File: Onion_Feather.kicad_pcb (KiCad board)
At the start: 2 copper layers, 50.8 x 53.3 mm, 2 parts, among them U1 Omega2+

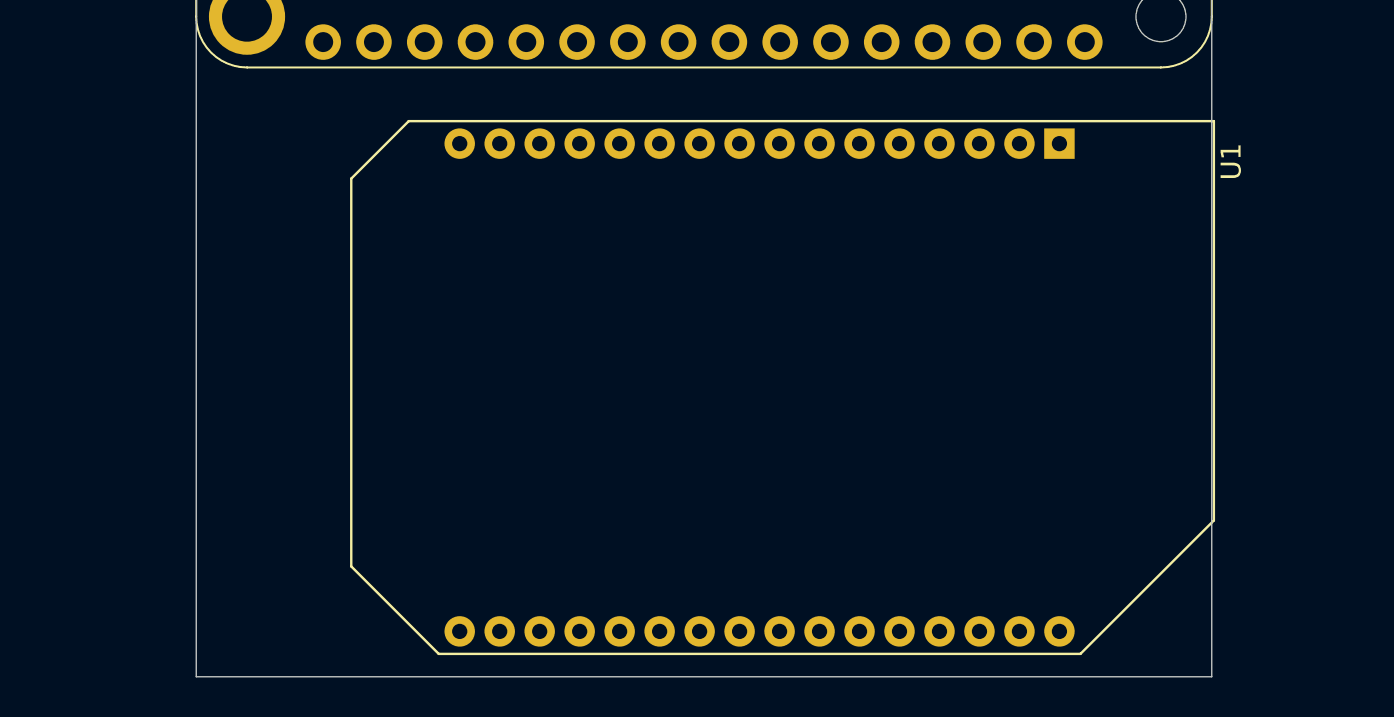
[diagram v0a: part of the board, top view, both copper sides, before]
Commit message: Add Hanrun magjack
Signed-off-by: Tisham Dhar <whatnickd@gmail.com>
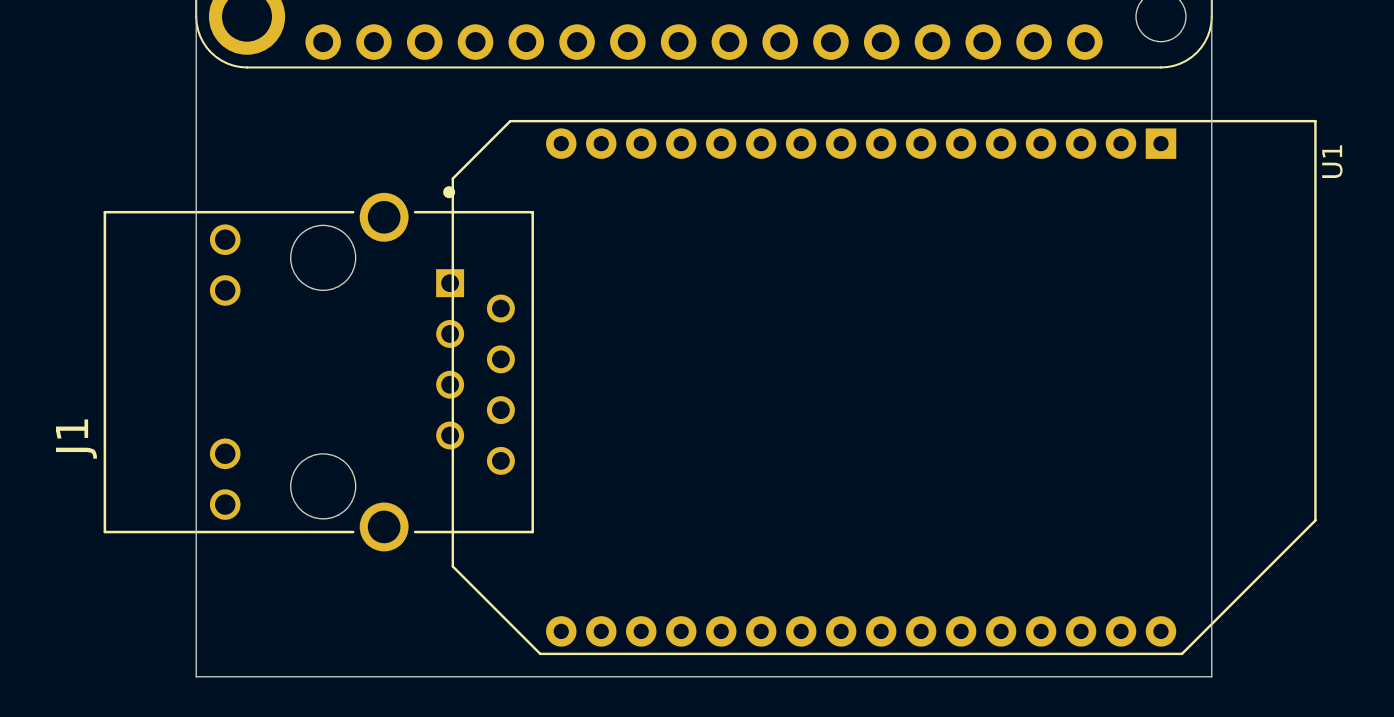
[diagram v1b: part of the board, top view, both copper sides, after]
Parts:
- added J1: HR911105A, footprints:HANRUN_HR911105A, F.Cu at (123.2, 99.1)
- moved U1 5.08 mm to (165.1, 87.6)
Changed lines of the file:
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@@
     (tracks 0)
     (zones 0)
-    (modules 2)
-    (nets 60)
+    (modules 3)
+    (nets 72)
   )
   (page A4)
@@
   (net 58 "Net-(U1-Pad3)")
   (net 59 "Net-(U1-Pad2)")
+  (net 60 "Net-(J1-Pad15)")
+  (net 61 "Net-(J1-Pad11)")
+  (net 62 "Net-(J1-Pad12)")
+  (net 63 "Net-(J1-Pad10)")
+  (net 64 "Net-(J1-Pad9)")
+  (net 65 "Net-(J1-Pad8)")
+  (net 66 "Net-(J1-Pad6)")
+  (net 67 "Net-(J1-Pad5)")
+  (net 68 "Net-(J1-Pad4)")
+  (net 69 "Net-(J1-Pad3)")
+  (net 70 "Net-(J1-Pad2)")
+  (net 71 "Net-(J1-Pad1)")
   (net_class Default "This is the default net class."
     (clearance 0.2)
@@
     (uvia_dia 0.3)
     (uvia_drill 0.1)
+    (add_net "Net-(J1-Pad1)")
+    (add_net "Net-(J1-Pad10)")
+    (add_net "Net-(J1-Pad11)")
+    (add_net "Net-(J1-Pad12)")
+    (add_net "Net-(J1-Pad15)")
+    (add_net "Net-(J1-Pad2)")
+    (add_net "Net-(J1-Pad3)")
+    (add_net "Net-(J1-Pad4)")
+    (add_net "Net-(J1-Pad5)")
+    (add_net "Net-(J1-Pad6)")
+    (add_net "Net-(J1-Pad8)")
+    (add_net "Net-(J1-Pad9)")
     (add_net "Net-(MS1-Pad1)")
     (add_net "Net-(MS1-Pad10)")
@@
     (add_net "Net-(U1-Pad9)")
   )
+  (module footprints:HANRUN_HR911105A (layer F.Cu)
+    (at 123.19 99.06 90)
+    (fp_text reference J1 (at -3.18815 -12.50276 90) (layer F.SilkS)
+      (effects (font (size 1.607654 1.607654) (thickness 0.015)))
+    )
+    (fp_text value HR911105A (at 8.02765 12.354385 90) (layer F.Fab)
+      (effects (font (size 1.605063 1.605063) (thickness 0.015)))
+    )
+    (fp_line (start 9.25 -11.17) (end -9.25 -11.17) (layer F.CrtYd) (width 0.05))
+    (fp_line (start 9.25 10.73) (end 9.25 -11.17) (layer F.CrtYd) (width 0.05))
+    (fp_line (start -9.25 10.73) (end 9.25 10.73) (layer F.CrtYd) (width 0.05))
+    (fp_line (start -9.25 -11.17) (end -9.25 10.73) (layer F.CrtYd) (width 0.05))
+    (fp_line (start 8 -10.92) (end -8 -10.92) (layer F.Fab) (width 0.127))
+    (fp_line (start 8 10.48) (end 8 -10.92) (layer F.Fab) (width 0.127))
+    (fp_line (start -8 10.48) (end 8 10.48) (layer F.Fab) (width 0.127))
+    (fp_line (start -8 -10.92) (end -8 10.48) (layer F.Fab) (width 0.127))
+    (fp_circle (center 9 6.3) (end 9.15 6.3) (layer F.SilkS) (width 0.3))
+    (fp_circle (center 5.8 6.3) (end 5.95 6.3) (layer F.Fab) (width 0.3))
+    (fp_line (start 8 4.6) (end 8 10.48) (layer F.SilkS) (width 0.127))
+    (fp_line (start 8 -10.92) (end 8 1.5) (layer F.SilkS) (width 0.127))
+    (fp_line (start -8 4.6) (end -8 10.48) (layer F.SilkS) (width 0.127))
+    (fp_line (start -8 -10.92) (end -8 1.5) (layer F.SilkS) (width 0.127))
+    (fp_line (start 8 -10.92) (end -8 -10.92) (layer F.SilkS) (width 0.127))
+    (fp_line (start 8 10.48) (end -8 10.48) (layer F.SilkS) (width 0.127))
+    (pad None np_thru_hole circle (at 5.715 0 90) (size 3.25 3.25) (drill 3.25) (layers *.Cu *.Mask))
+    (pad None np_thru_hole circle (at -5.715 0 90) (size 3.25 3.25) (drill 3.25) (layers *.Cu *.Mask))
+    (pad 16 thru_hole circle (at -7.745 3.05 90) (size 2.445 2.445) (drill 1.63) (layers *.Cu *.Mask)
+      (net 60 "Net-(J1-Pad15)"))
+    (pad 15 thru_hole circle (at 7.745 3.05 90) (size 2.445 2.445) (drill 1.63) (layers *.Cu *.Mask)
+      (net 60 "Net-(J1-Pad15)"))
+    (pad 11 thru_hole circle (at -4.085 -4.9 90) (size 1.53 1.53) (drill 1.02) (layers *.Cu *.Mask)
+      (net 61 "Net-(J1-Pad11)"))
+    (pad 12 thru_hole circle (at -6.625 -4.9 90) (size 1.53 1.53) (drill 1.02) (layers *.Cu *.Mask)
+      (net 62 "Net-(J1-Pad12)"))
+    (pad 10 thru_hole circle (at 4.085 -4.9 90) (size 1.53 1.53) (drill 1.02) (layers *.Cu *.Mask)
+      (net 63 "Net-(J1-Pad10)"))
+    (pad 9 thru_hole circle (at 6.625 -4.9 90) (size 1.53 1.53) (drill 1.02) (layers *.Cu *.Mask)
+      (net 64 "Net-(J1-Pad9)"))
+    (pad 8 thru_hole circle (at -4.44 8.89 90) (size 1.398 1.398) (drill 0.89) (layers *.Cu *.Mask)
+      (net 65 "Net-(J1-Pad8)"))
+    (pad 7 thru_hole circle (at -3.17 6.35 90) (size 1.398 1.398) (drill 0.89) (layers *.Cu *.Mask))
+    (pad 6 thru_hole circle (at -1.9 8.89 90) (size 1.398 1.398) (drill 0.89) (layers *.Cu *.Mask)
+      (net 66 "Net-(J1-Pad6)"))
+    (pad 5 thru_hole circle (at -0.63 6.35 90) (size 1.398 1.398) (drill 0.89) (layers *.Cu *.Mask)
+      (net 67 "Net-(J1-Pad5)"))
+    (pad 4 thru_hole circle (at 0.64 8.89 90) (size 1.398 1.398) (drill 0.89) (layers *.Cu *.Mask)
+      (net 68 "Net-(J1-Pad4)"))
+    (pad 3 thru_hole circle (at 1.91 6.35 90) (size 1.398 1.398) (drill 0.89) (layers *.Cu *.Mask)
+      (net 69 "Net-(J1-Pad3)"))
+    (pad 2 thru_hole circle (at 3.18 8.89 90) (size 1.398 1.398) (drill 0.89) (layers *.Cu *.Mask)
+      (net 70 "Net-(J1-Pad2)"))
+    (pad 1 thru_hole rect (at 4.45 6.35 90) (size 1.398 1.398) (drill 0.89) (layers *.Cu *.Mask)
+      (net 71 "Net-(J1-Pad1)"))
+  )
   (module Module:Onion_Omega2+ (layer F.Cu)
-    (at 160.02 87.63 270)
+    (at 165.1 87.63 270)
     (descr https://onion.io/omega2/)
     (tags "Omega Onion module")

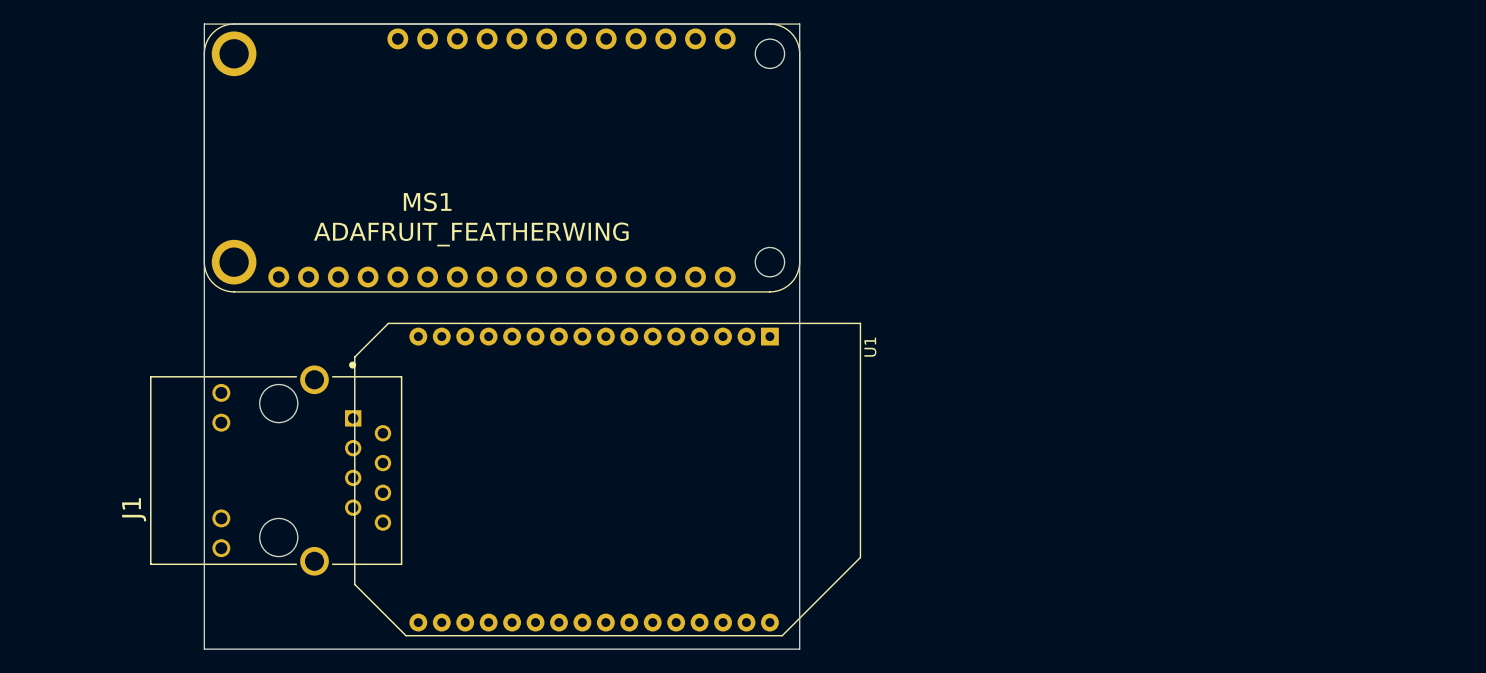
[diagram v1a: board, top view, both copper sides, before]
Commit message: Try Hanrun magjack on for size
Signed-off-by: Tisham Dhar <whatnickd@gmail.com>
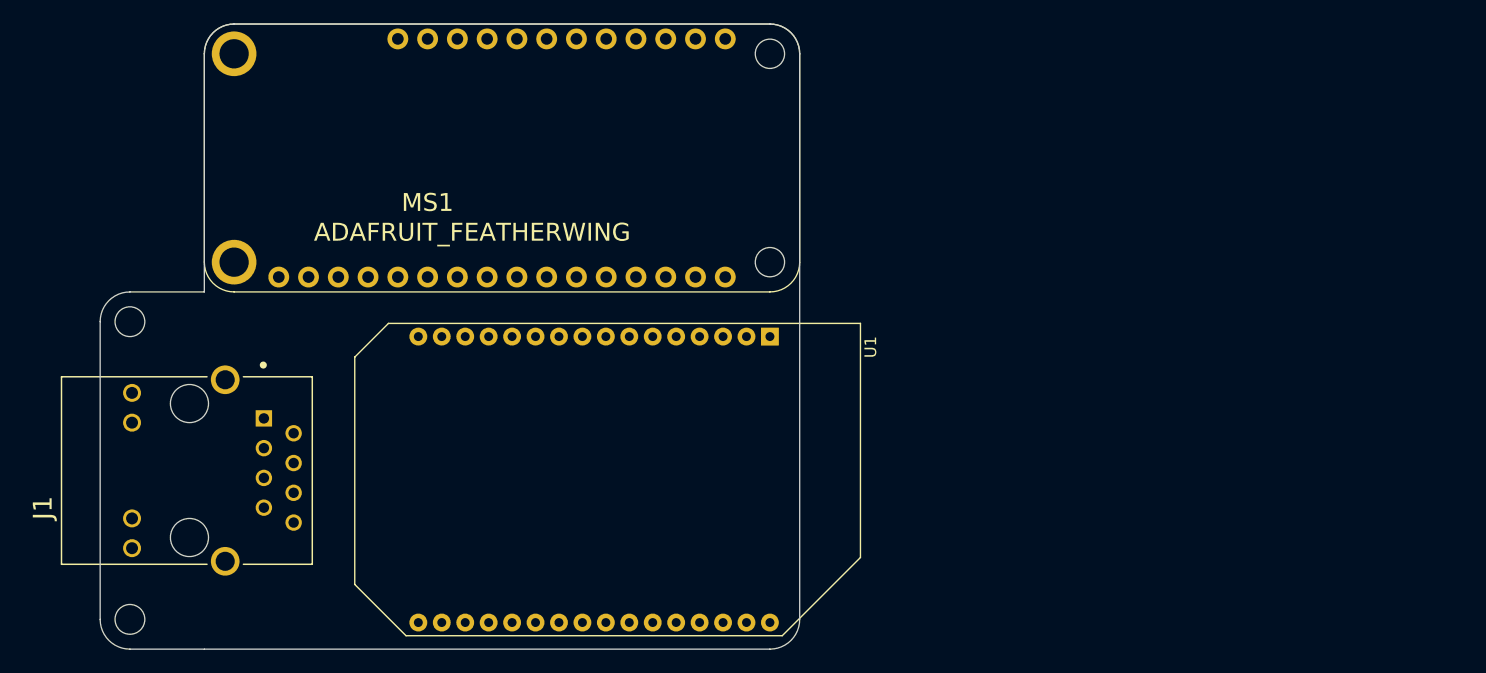
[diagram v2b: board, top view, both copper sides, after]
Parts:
- moved J1 7.62 mm to (115.6, 99.1)
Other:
- board size 50.8 x 53.3 mm -> 59.7 x 53.3 mm
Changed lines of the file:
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@@
   (general
     (thickness 1.6)
-    (drawings 6)
+    (drawings 16)
     (tracks 0)
     (zones 0)
@@
     (35 F.Paste user)
     (36 B.SilkS user)
-    (37 F.SilkS user)
+    (37 F.SilkS user hide)
     (38 B.Mask user)
     (39 F.Mask user)
-    (40 Dwgs.User user)
+    (40 Dwgs.User user hide)
     (41 Cmts.User user)
     (42 Eco1.User user)
@@
   )
   (module footprints:HANRUN_HR911105A (layer F.Cu)
-    (at 123.19 99.06 90)
+    (at 115.57 99.06 90)
     (fp_text reference J1 (at -3.18815 -12.50276 90) (layer F.SilkS)
       (effects (font (size 1.607654 1.607654) (thickness 0.015)))
@@
     (pad 1 thru_hole rect (at 4.45 6.35 90) (size 1.398 1.398) (drill 0.89) (layers *.Cu *.Mask)
       (net 71 "Net-(J1-Pad1)"))
+    (model ${KIPRJMOD}/3dmodels/RJ45_Hanrun_HR911105A.wrl
+      (offset (xyz 4.5 -6.5 0))
+      (scale (xyz 1 1 1))
+      (rotate (xyz 0 0 180))
+    )
   )
   (module Module:Onion_Omega2+ (layer F.Cu)
@@
       (net 28 "Net-(MS1-Pad1)"))
   )
+  (gr_circle (center 110.49 111.76) (end 110.49 110.49) (layer Edge.Cuts) (width 0.05))
+  (gr_circle (center 110.49 86.36) (end 110.49 85.09) (layer Edge.Cuts) (width 0.05))
+  (gr_arc (start 110.49 86.36) (end 110.49 83.82) (angle -90) (layer Edge.Cuts) (width 0.05))
+  (gr_arc (start 110.49 111.76) (end 107.95 111.76) (angle -90) (layer Edge.Cuts) (width 0.05))
+  (gr_arc (start 165.1 111.76) (end 165.1 114.3) (angle -90) (layer Edge.Cuts) (width 0.05))
+  (gr_arc (start 165.1 63.5) (end 167.64 63.5) (angle -90) (layer Edge.Cuts) (width 0.05))
+  (gr_arc (start 119.38 63.5) (end 119.38 60.96) (angle -90) (layer Edge.Cuts) (width 0.05))
+  (gr_line (start 110.49 114.3) (end 116.84 114.3) (layer Edge.Cuts) (width 0.05))
+  (gr_line (start 107.95 86.36) (end 107.95 111.76) (layer Edge.Cuts) (width 0.05))
+  (gr_line (start 116.84 83.82) (end 110.49 83.82) (layer Edge.Cuts) (width 0.05))
   (dimension 50.8 (width 0.15) (layer Dwgs.User)
     (gr_text "50.800 mm" (at 142.24 52.04) (layer Dwgs.User)
@@
     (arrow2b (pts (xy 177.8 60.96) (xy 178.386421 62.086504)))
   )
-  (gr_line (start 167.64 60.96) (end 116.84 60.96) (layer Edge.Cuts) (width 0.05))
-  (gr_line (start 167.64 114.3) (end 167.64 60.96) (layer Edge.Cuts) (width 0.05))
-  (gr_line (start 116.84 114.3) (end 167.64 114.3) (layer Edge.Cuts) (width 0.05))
-  (gr_line (start 116.84 60.96) (end 116.84 114.3) (layer Edge.Cuts) (width 0.05))
+  (gr_line (start 165.1 60.96) (end 119.38 60.96) (layer Edge.Cuts) (width 0.05))
+  (gr_line (start 167.64 111.76) (end 167.64 63.5) (layer Edge.Cuts) (width 0.05))
+  (gr_line (start 116.84 114.3) (end 165.1 114.3) (layer Edge.Cuts) (width 0.05))
+  (gr_line (start 116.84 63.5) (end 116.84 83.82) (layer Edge.Cuts) (width 0.05))
 )

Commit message: Importing prior art from Eagle
Signed-off-by: Tisham Dhar <whatnickd@gmail.com>
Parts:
- added C1: 10uF, Capacitor_SMD:C_0805_2012Metric, F.Cu at (213.9, 84.3)
- added C2: 10uF, Capacitor_SMD:C_0805_2012Metric, F.Cu at (193.9, 97.3)
- added FTDI1: CON_HEADER_1X06-PTH, Connector_PinHeader_2.54mm:PinHeader_1x06_P2.54mm_Horizontal, F.Cu at (187.3, 72.9)
- added I2C1: M04PTH, Connector_PinHeader_2.54mm:PinHeader_1x04_P2.54mm_Horizontal, F.Cu at (214.1, 72.9)
- added J2: CON_HEADER_PRG_AVR_ICSP-PTH, Connector_PinSocket_2.54mm:PinSocket_2x03_P2.54mm_Vertical, F.Cu at (201.2, 90.3)
- added JP1: JUMPER2, Jumper:SolderJumper-2_P1.3mm_Bridged_RoundedPad1.0x1.5mm, F.Cu at (191.5, 103.7)
- added P1: PADNORMAL, TestPoint:TestPoint_Pad_D1.0mm, F.Cu at (186.5, 106.4)
- added P2: PADNORMAL, TestPoint:TestPoint_Pad_D1.0mm, F.Cu at (193.2, 100.3)
- added PTH1: CON_HEADER_1X06, Connector_PinHeader_2.54mm:PinHeader_1x06_P2.54mm_Horizontal, F.Cu at (200.7, 72.9)
- added R1: 4.7K, Resistor_SMD:R_0805_2012Metric, F.Cu at (187.1, 103.4)
- added R2: 4.7K, Resistor_SMD:R_0805_2012Metric, F.Cu at (205.7, 89.4)
- added U2: CJ1117 3V3, Package_TO_SOT_SMD:SOT-89-3, F.Cu at (187.9, 98.9)
- added USB1: USB_POWER, Connector_USB:USB_Micro-AB_Molex_47590-0001, F.Cu at (118.3, 72.4)
- U1: value Omega2+ -> ONION-OMEGA2
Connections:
- U1 pad 1: Net-(U1-Pad1) -> (no net)
- U1 pad 10: Net-(U1-Pad10) -> (no net)
- U1 pad 11: Net-(U1-Pad11) -> (no net)
- U1 pad 12: Net-(U1-Pad12) -> (no net)
- U1 pad 13: Net-(U1-Pad13) -> (no net)
- U1 pad 14: Net-(U1-Pad14) -> (no net)
- U1 pad 15: Net-(U1-Pad15) -> (no net)
- U1 pad 16: Net-(U1-Pad16) -> (no net)
- U1 pad 17: Net-(U1-Pad17) -> (no net)
- U1 pad 18: Net-(U1-Pad18) -> (no net)
- U1 pad 19: Net-(U1-Pad19) -> (no net)
- U1 pad 2: Net-(U1-Pad2) -> (no net)
- U1 pad 20: Net-(U1-Pad20) -> (no net)
- U1 pad 21: Net-(U1-Pad21) -> (no net)
- U1 pad 22: Net-(U1-Pad22) -> (no net)
- U1 pad 23: Net-(U1-Pad23) -> (no net)
- U1 pad 24: Net-(U1-Pad24) -> (no net)
- U1 pad 25: Net-(U1-Pad25) -> (no net)
- U1 pad 26: Net-(U1-Pad26) -> (no net)
- U1 pad 27: Net-(U1-Pad27) -> (no net)
- U1 pad 28: Net-(U1-Pad28) -> (no net)
- U1 pad 29: Net-(U1-Pad29) -> (no net)
- U1 pad 3: Net-(U1-Pad3) -> (no net)
- U1 pad 30: Net-(U1-Pad30) -> (no net)
- U1 pad 31: Net-(U1-Pad31) -> (no net)
- U1 pad 32: Net-(U1-Pad1) -> (no net)
- U1 pad 4: Net-(U1-Pad4) -> (no net)
- U1 pad 5: Net-(U1-Pad5) -> (no net)
- U1 pad 6: Net-(U1-Pad6) -> (no net)
- U1 pad 7: Net-(U1-Pad7) -> (no net)
- U1 pad 8: Net-(U1-Pad8) -> (no net)
- U1 pad 9: Net-(U1-Pad9) -> (no net)
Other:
- outline, holes or cut-outs redrawn

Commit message: Added more features and 3D models
Signed-off-by: Tisham Dhar <whatnickd@gmail.com>
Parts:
- added J3: Conn_01x02, Connector_JST:JST_PH_S2B-PH-SM4-TB_1x02-1MP_P2.00mm_Horizontal, F.Cu at (127.2, 65.9)
- added J4: USB_A, footprints:67643-0910, F.Cu at (170.2, 79.6)
- added U3: CP2102N-A01-GQFN24, Package_DFN_QFN:QFN-24-1EP_4x4mm_P0.5mm_EP2.6x2.6mm, F.Cu at (135.7, 72.6)
- I2C1: footprint Connector_PinHeader_2.54mm:PinHeader_1x04_P2.54mm_Horizontal -> Connector_JST:JST_SH_SM04B-SRSS-TB_1x04-1MP_P1.00mm_Horizontal
- J2: footprint Connector_PinSocket_2.54mm:PinSocket_2x03_P2.54mm_Vertical -> Connector_JST:JST_SH_SM06B-SRSS-TB_1x06-1MP_P1.00mm_Horizontal
- USB1: value USB_POWER -> USB_B_Micro
- moved C1 80.4 mm to (133.7, 79.0)
- moved C2 72.1 mm to (124.1, 78.9)
- moved U2 62.7 mm to (129.0, 77.5), turned to 90 degrees
- moved I2C1 53.8 mm to (164.3, 93.5), turned to 90 degrees
- moved P1 39.3 mm to (179.6, 67.7)
- moved J2 39.2 mm to (164.3, 103.6), turned to 90 degrees
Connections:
- U1 pad 1: (no net) -> GND
- U1 pad 10: (no net) -> /OnionModule/MISO
- U1 pad 11: (no net) -> /OnionModule/MOSI
- U1 pad 12: (no net) -> /OnionModule/CLK
- U1 pad 13: (no net) -> /OnionModule/CS
- U1 pad 14: (no net) -> Net-(U1-Pad14)
- U1 pad 15: (no net) -> Net-(U1-Pad15)
- U1 pad 16: (no net) -> Net-(U1-Pad16)
- U1 pad 17: (no net) -> /OnionModule/SDA
- U1 pad 18: (no net) -> /OnionModule/SCL
- U1 pad 19: (no net) -> Net-(U1-Pad19)
- U1 pad 2: (no net) -> Net-(U1-Pad2)
- U1 pad 20: (no net) -> Net-(U1-Pad20)
- U1 pad 21: (no net) -> Net-(U1-Pad21)
- U1 pad 22: (no net) -> Net-(U1-Pad22)
- U1 pad 23: (no net) -> Net-(U1-Pad23)
- U1 pad 24: (no net) -> Net-(U1-Pad24)
- U1 pad 25: (no net) -> Net-(U1-Pad25)
- U1 pad 26: (no net) -> Net-(U1-Pad26)
- U1 pad 27: (no net) -> /OnionModule/TX
- U1 pad 28: (no net) -> /OnionModule/RX
- U1 pad 29: (no net) -> Net-(U1-Pad29)
- U1 pad 3: (no net) -> Net-(U1-Pad3)
- U1 pad 30: (no net) -> Net-(U1-Pad30)
- U1 pad 31: (no net) -> 3.3V
- U1 pad 32: (no net) -> GND
- U1 pad 4: (no net) -> Net-(U1-Pad4)
- U1 pad 5: (no net) -> Net-(U1-Pad5)
- U1 pad 6: (no net) -> Net-(U1-Pad6)
- U1 pad 7: (no net) -> Net-(U1-Pad7)
- U1 pad 8: (no net) -> Net-(U1-Pad8)
- U1 pad 9: (no net) -> Net-(U1-Pad9)
- USB1 pad 1: (no net) -> VIN
- USB1 pad 2: (no net) -> GND
- USB1 pad 3: (no net) -> Net-(USB1-Pad3)
- USB1 pad 4: (no net) -> Net-(USB1-Pad4)
- USB1 pad 5: (no net) -> GND
- USB1 pad 6: (no net) -> Net-(USB1-Pad6)
